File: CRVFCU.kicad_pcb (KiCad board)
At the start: 4 copper layers, 50 x 100 mm, 151 parts, among them J1 TagConnect_TC2030, J2 Conn_01x02, J3 USB_C_Receptacle_USB2.0_16P, J4 Micro_SD_Card_Det2, J5 Conn_01x02, Q3 DMG2301L, Q4 BC818, Q5 DMG2301L, Q6 DMG2301L, U1 MS5611-01BA, U10 W25Q128JVS, U11 EClamp2515K, U12 ESDALC6V1W5, U13 USBLC6-2SC6, U14 USBLC6-2SC6, U15 MAX17049, U16 SI7232DN-T1, U17 SN74LV1T34DCK, U2 STM32H747IITx, U3 LIS2MDL, U4 ICM-45686, U5 FXMA108, U6 AP1117-50, U7 AP1117-33, U8 SI7232DN-T1, U9 USBLC6-4SC6, Y1 32.768khz, Y2 Crystal_GND24, Y3 32.768khz

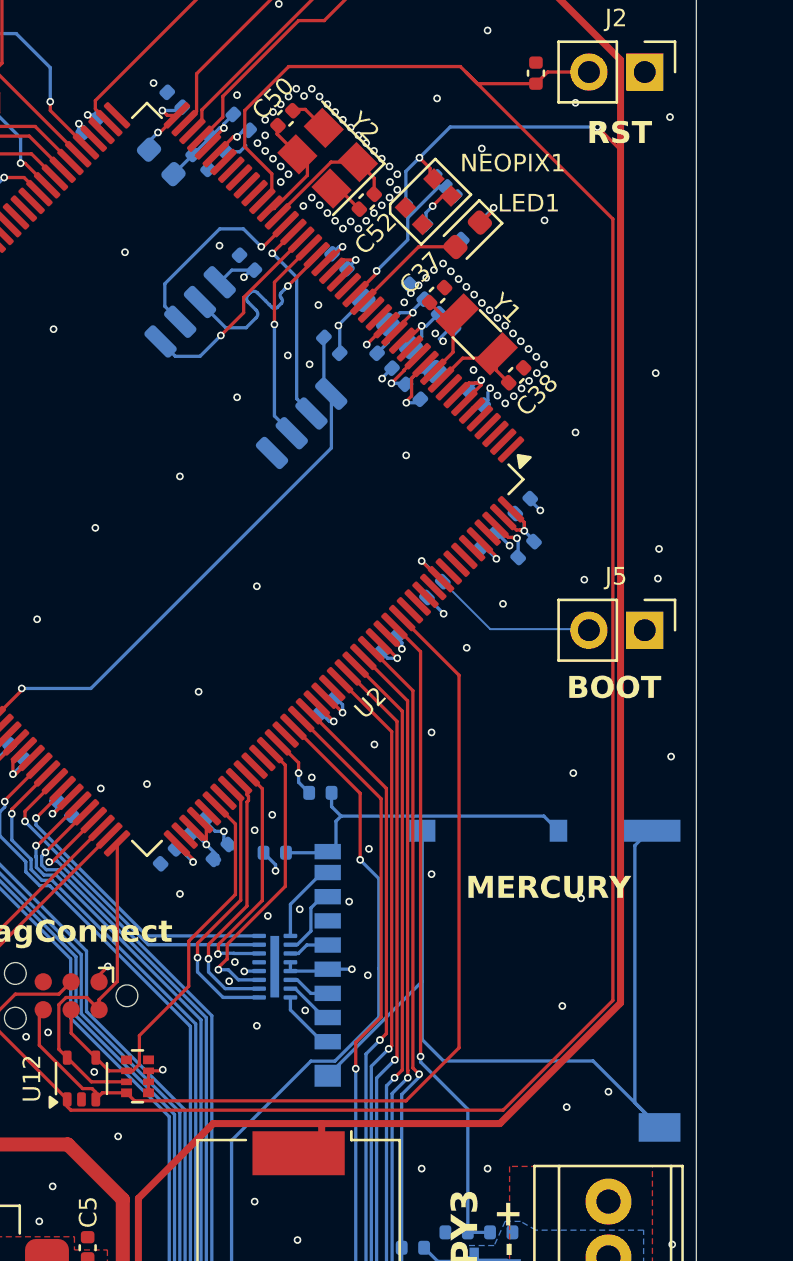
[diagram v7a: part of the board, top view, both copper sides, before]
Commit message: added vref caps and changed some cap values
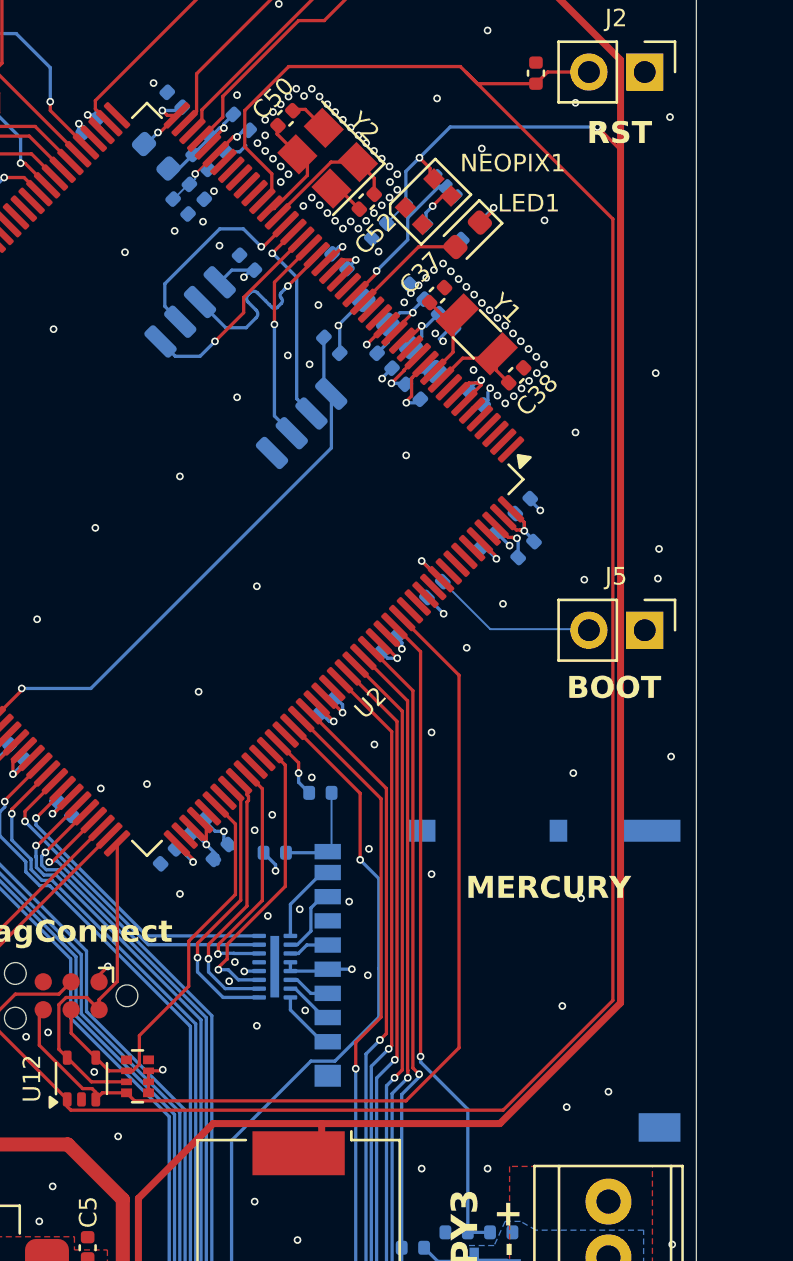
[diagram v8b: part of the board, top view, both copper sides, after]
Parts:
- added C53: 100nF, Capacitor_SMD:C_0402_1005Metric, B.Cu at (75.6, 42.8)
- added C54: 1uF, Capacitor_SMD:C_0402_1005Metric, B.Cu at (66.5, 41.7)
- added C55: 100nF, Capacitor_SMD:C_0402_1005Metric, B.Cu at (67.3, 41.0)
- C17: value 10uF -> 1uF
- moved L1 0.34 mm to (65.4, 39.4)
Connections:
- net Net-(U2-VREF+) renamed /VREF
- J4 pad 10: Net-(J4-DET_A) -> GND
- J4 pad 11: unconnected-(J4-SHIELD-Pad11) -> GND
- J4 pad 9: Net-(J4-DET_A) -> Net-(J4-DET_B)
- R24 pad 2: Net-(J4-DET_A) -> Net-(J4-DET_B)
- R46 pad 2: Net-(J4-DET_A) -> Net-(J4-DET_B)
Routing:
- net unconnected-(J4-SHIELD-Pad11): track 42.3 -> 0.00 mm
- net Net-(J4-DET_A): track 15.4 -> 0.00 mm
- net Net-(J4-DET_B): track 0.00 -> 4.92 mm
- net /VREF: track 1.96 -> 5.07 mm, vias 1 -> 2
- net +5V: track 134.6 -> 135.8 mm
- net GND: vias 230 -> 234
